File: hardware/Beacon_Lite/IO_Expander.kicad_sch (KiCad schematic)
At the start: 6 parts, among them U3 PI4IOE5V96248ZLEX

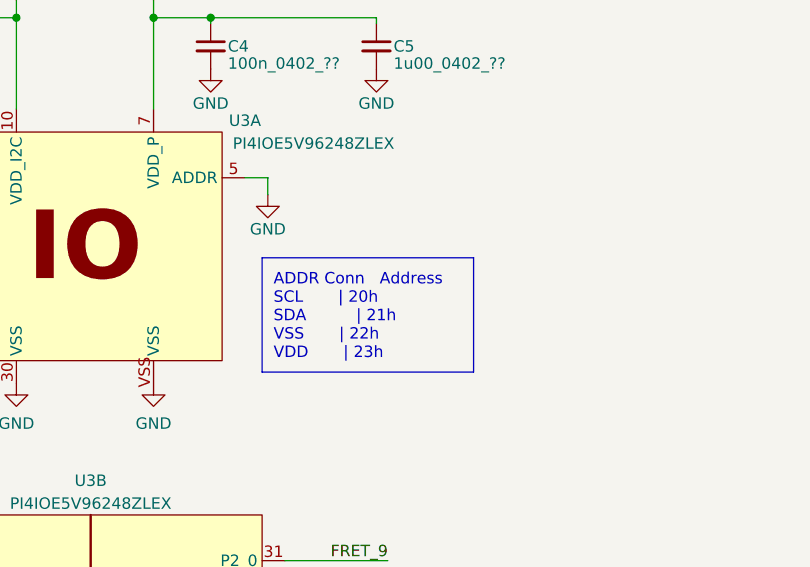
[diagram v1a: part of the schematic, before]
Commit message: Started programming NUCLEO-H533 in VSCODE
* Able to use C++ and C
* Successful able to debug
* Can blink an LED when button is pressed via an interrupt.
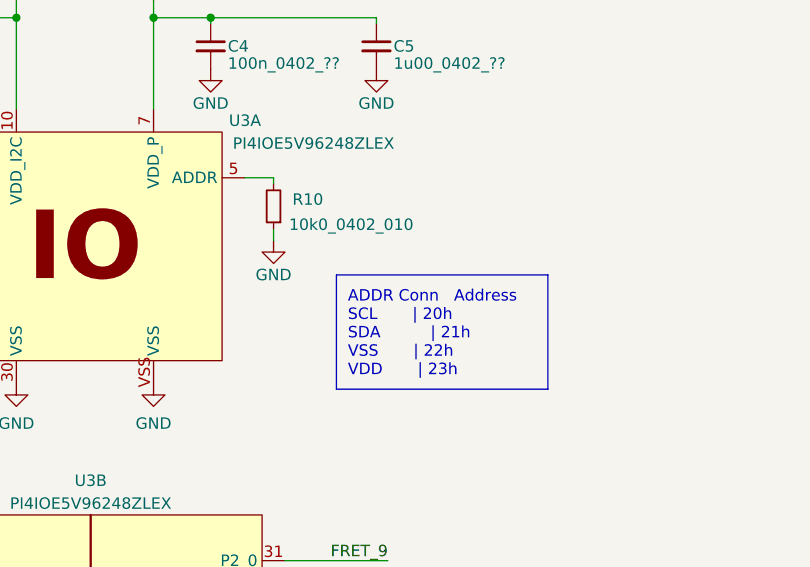
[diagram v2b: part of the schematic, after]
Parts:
- added R10: 10k0_0402_010, Footprint_Library:0402_1005Metric_Handsolder, symbol Device:R_Small
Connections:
- net GND: now also R10.1; no longer U3.5 (ADDR)
- new net: R10.2, U3.5 (ADDR)
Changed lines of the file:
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@@
 	)
 	(rectangle
-		(start 88.9 59.055)
-		(end 112.395 71.755)
+		(start 97.155 60.96)
+		(end 120.65 73.66)
 		(stroke
 			(width 0)
@@
 	(text "ADDR Conn   Address\nSCL 	  | 20h\nSDA		  | 21h\nVSS 	  | 22h\nVDD 	  | 23h"
 		(exclude_from_sim no)
-		(at 90.17 70.485 0)
+		(at 98.425 72.39 0)
 		(effects
 			(font
@@
 	(wire
 		(pts
-			(xy 89.535 52.07) (xy 89.535 50.165)
+			(xy 90.17 57.15) (xy 90.17 55.88)
 		)
 		(stroke
@@
 	(wire
 		(pts
+			(xy 90.17 50.8) (xy 90.17 50.165)
+		)
+		(stroke
+			(width 0)
+			(type default)
+		)
+	)
+	(wire
+		(pts
 			(xy 37.465 107.95) (xy 48.26 107.95)
 		)
@@
 	(wire
 		(pts
-			(xy 89.535 50.165) (xy 86.995 50.165)
+			(xy 90.17 50.165) (xy 86.995 50.165)
 		)
 		(stroke
@@
 	(symbol
 		(lib_id "power:GND")
-		(at 89.535 52.07 0)
+		(at 90.17 57.15 0)
 		(unit 1)
 		(exclude_from_sim no)
@@
 		(dnp no)
 		(property "Reference" "#PWR08"
-			(at 89.535 58.42 0)
+			(at 90.17 63.5 0)
 			(effects
 				(font
@@
 		)
 		(property "Value" "GND"
-			(at 89.535 55.88 0)
+			(at 90.17 60.96 0)
 			(effects
 				(font
@@
 		)
 		(property "Footprint" ""
-			(at 89.535 52.07 0)
+			(at 90.17 57.15 0)
 			(effects
 				(font
@@
 		)
 		(property "Datasheet" ""
-			(at 89.535 52.07 0)
+			(at 90.17 57.15 0)
 			(effects
 				(font
@@
 		)
 		(property "Description" ""
-			(at 89.535 52.07 0)
+			(at 90.17 57.15 0)
 			(effects
 				(font
@@
 					(unit 1)
 				)
+			)
+		)
+	)
+	(symbol
+		(lib_id "Device:R_Small")
+		(at 90.17 53.34 180)
+		(unit 1)
+		(exclude_from_sim no)
+		(in_bom yes)
+		(on_board yes)
+		(dnp no)
+		(property "Reference" "R10"
+			(at 93.98 52.578 0)
+			(effects
+				(font
+					(size 1.27 1.27)
+				)
+			)
+		)
+		(property "Value" "10k0_0402_010"
+			(at 98.806 55.372 0)
+			(effects
+				(font
+					(size 1.27 1.27)
+				)
+			)
+		)
+		(property "Footprint" "Footprint_Library:0402_1005Metric_Handsolder"
+			(at 90.17 53.34 0)
+			(effects
+				(font
+					(size 1.27 1.27)
+				)
+				(hide yes)
+			)
+		)
+		(property "Datasheet" "~"
+			(at 90.17 53.34 0)
+			(effects
+				(font
+					(size 1.27 1.27)
+				)
+				(hide yes)
+			)
+		)
+		(property "Description" ""
+			(at 90.17 53.34 0)
+			(effects
+				(font
+					(size 1.27 1.27)
+				)
+			)
+		)
+		(pin "1"
+		)
+		(pin "2"
+		)
+		(instances
+			(project "Beacon_Lite"
+				(path "/33ebacd6-2d94-4d95-bf8a-b8a1895869c6/7b6909ac-321e-415f-96bf-575349b8cc37"
+					(reference "R10")
+					(unit 1)
+				)
